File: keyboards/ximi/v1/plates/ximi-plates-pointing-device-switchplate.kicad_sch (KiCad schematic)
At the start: 31 parts, among them J2 USB_C_Receptacle_USB2.0, J7 AudioJack4dpb, SW1 SW_Push, SW10 SW_Push, SW11 SW_Push, SW12 SW_Push, SW13 SW_Push, SW14 SW_Push, SW15 SW_Push, SW16 SW_Push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

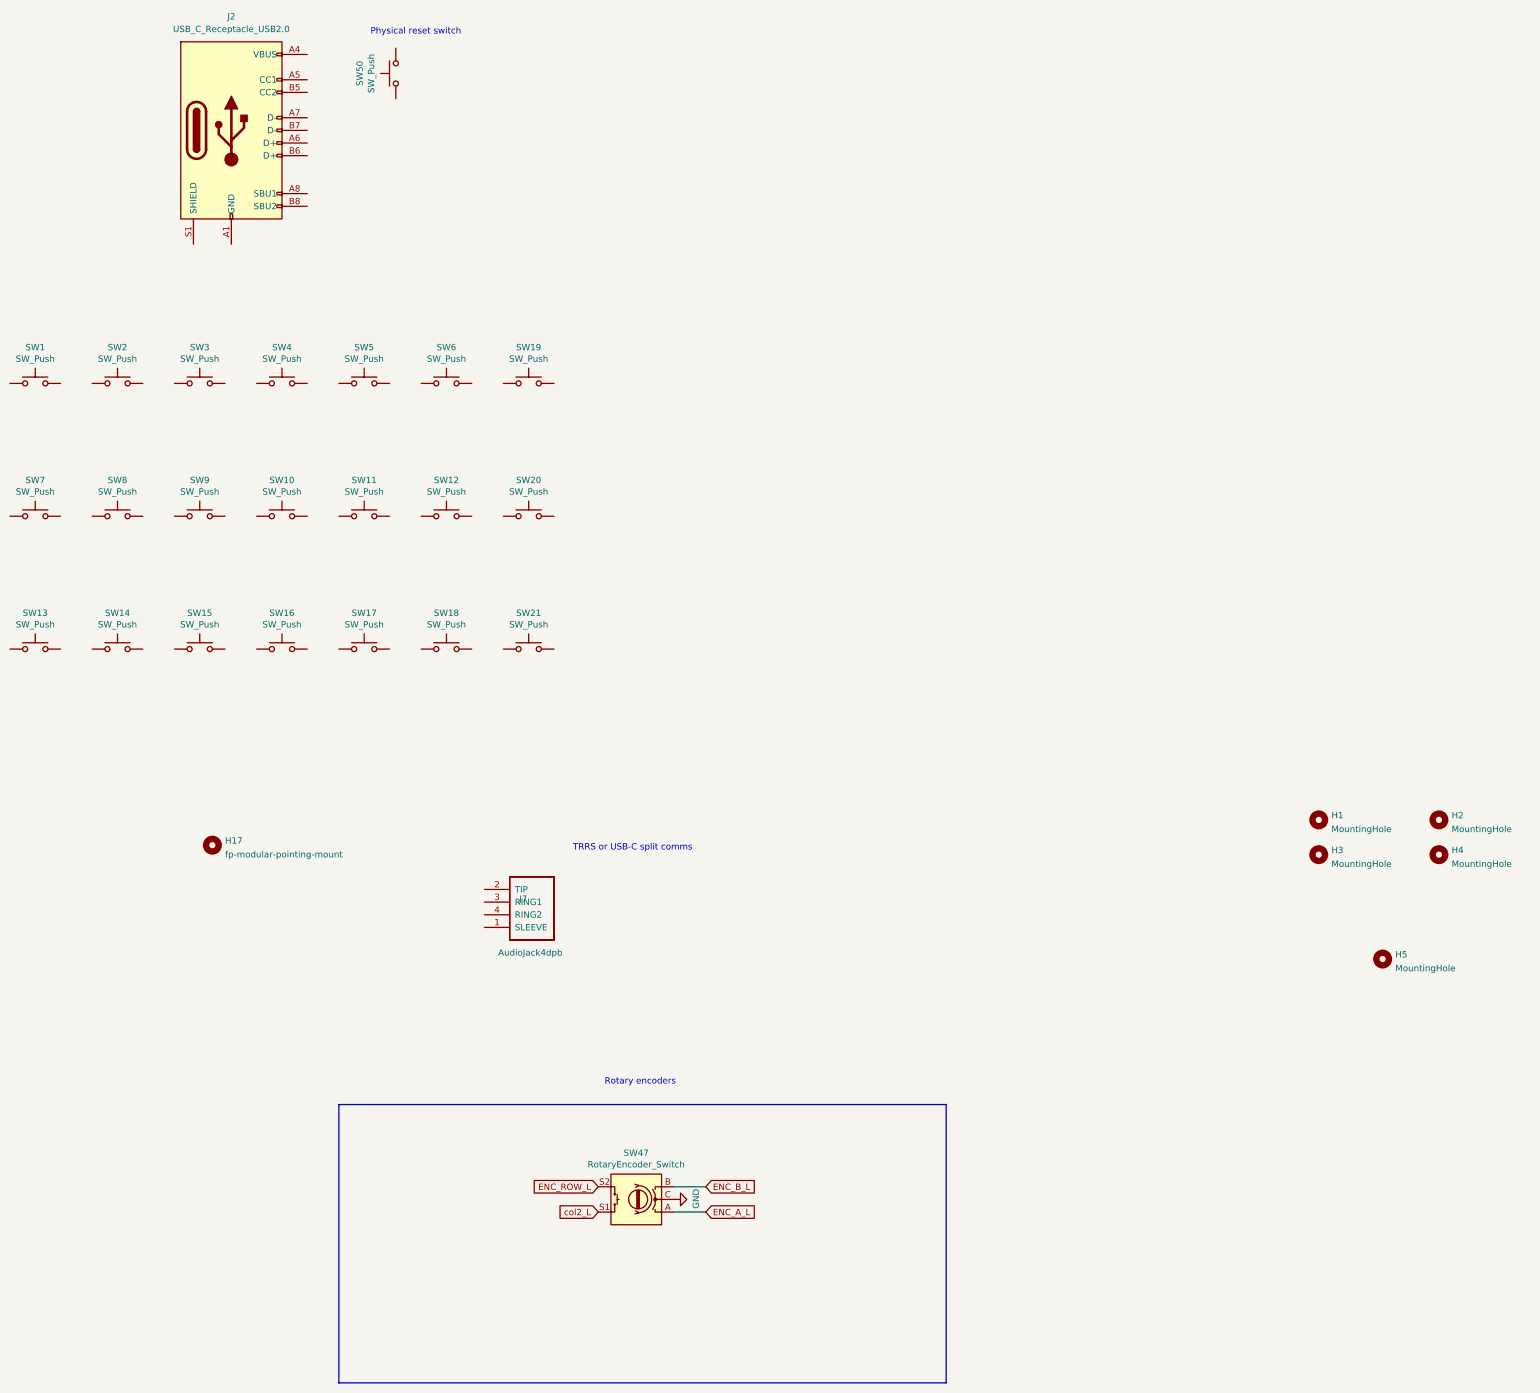
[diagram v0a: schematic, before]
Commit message: finished up basic pointing device plates, along with the templates
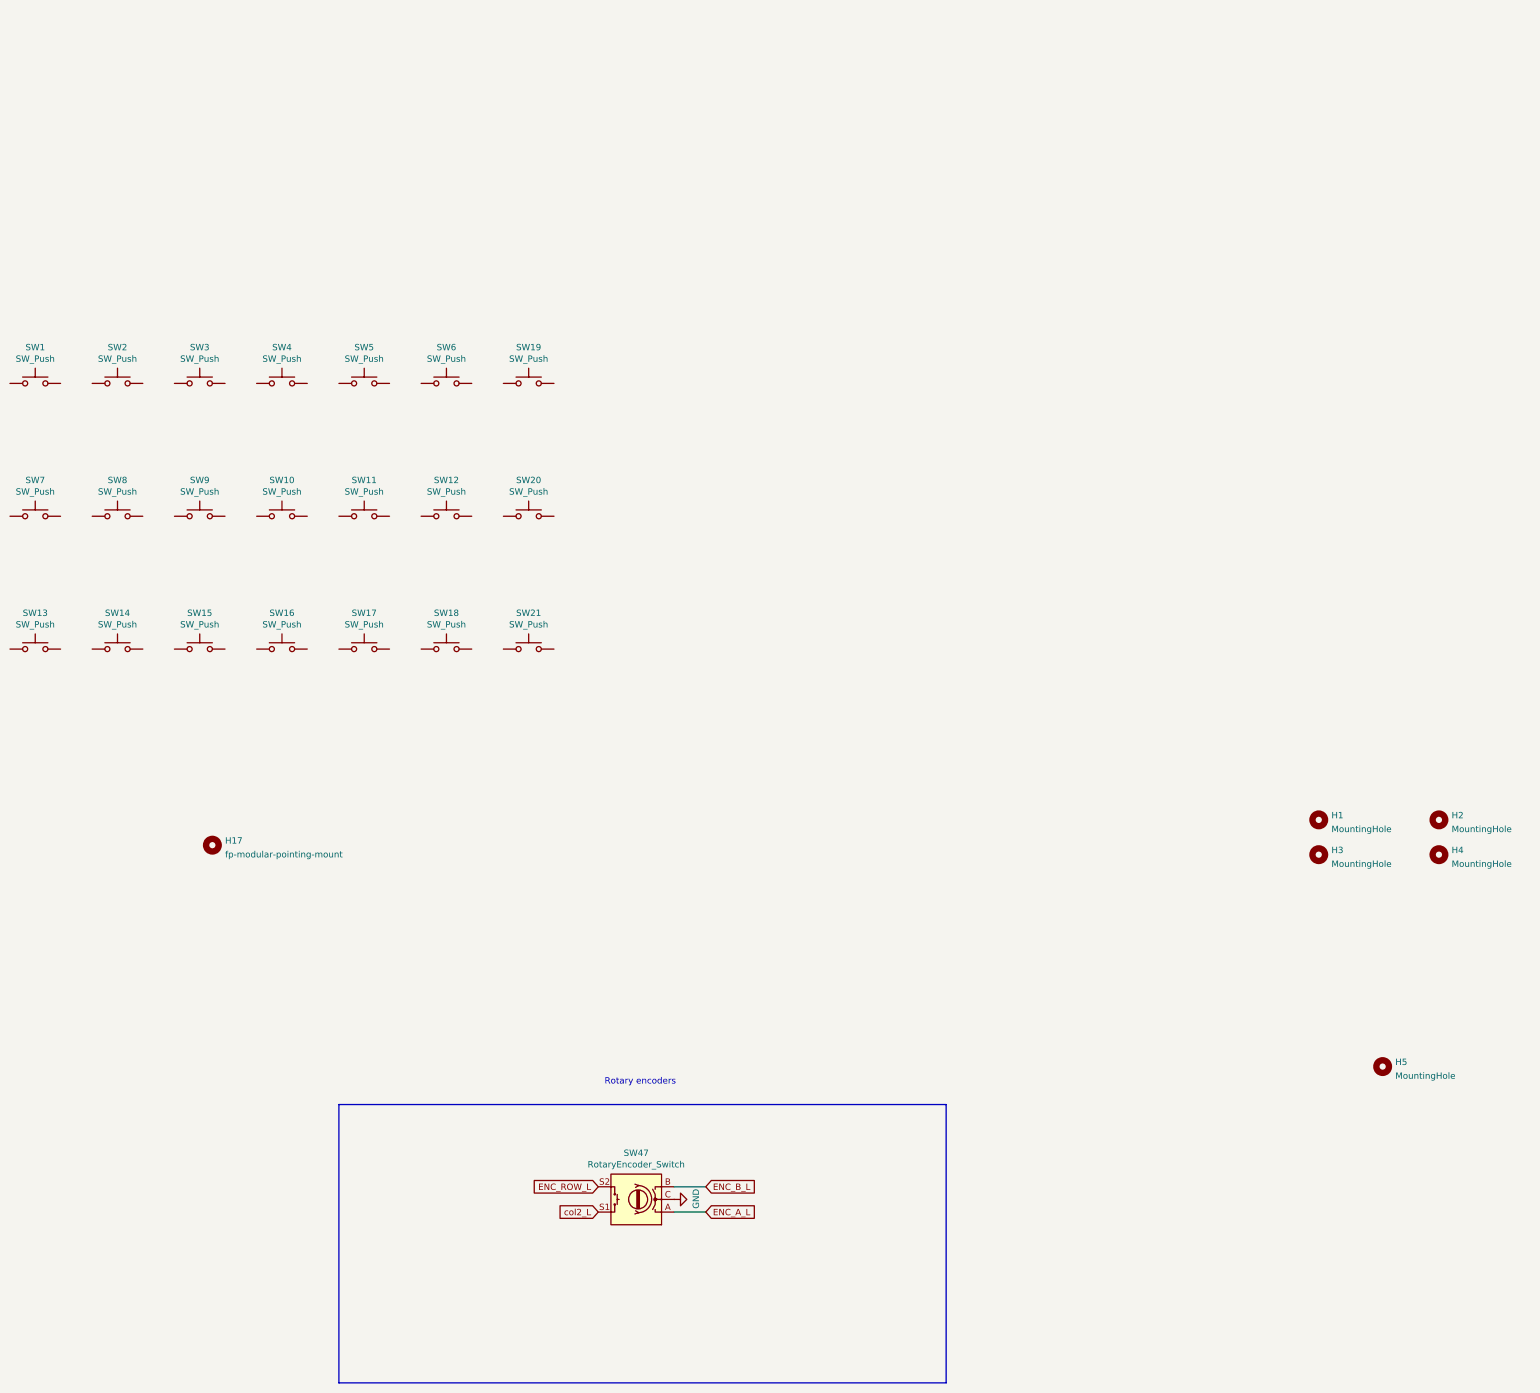
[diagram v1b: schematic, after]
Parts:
- removed J2: USB_C_Receptacle_USB2.0, fingerpunch-plates:USB_C_Receptacle_HRO_TYPE-C-31-M-12, symbol Connector:USB_C_Receptacle_USB2.0
- removed J7: AudioJack4dpb, fingerpunch-plates:TRRS-PJ-320A, symbol keebio:TRRS
- removed SW50: SW_Push, fingerpunch-plates:MountingHole_2.5mm, symbol Switch:SW_Push
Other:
- note removed: "Physical reset switch"
- note removed: "TRRS or USB-C split comms"
